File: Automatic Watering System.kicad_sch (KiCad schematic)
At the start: 6 parts, among them J1 691137710002, J2 691137710002, U1 DFR0654

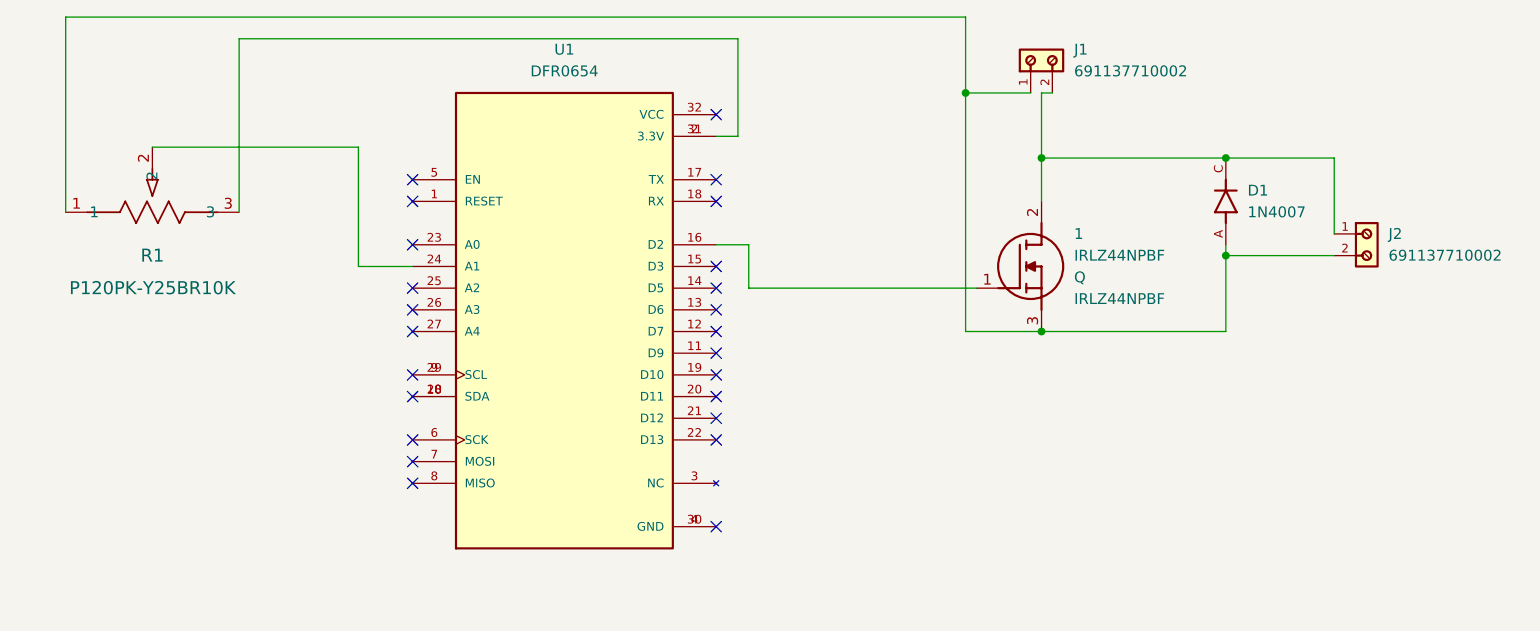
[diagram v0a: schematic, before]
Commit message: Fixing some issues with schematics and changing potentiometer
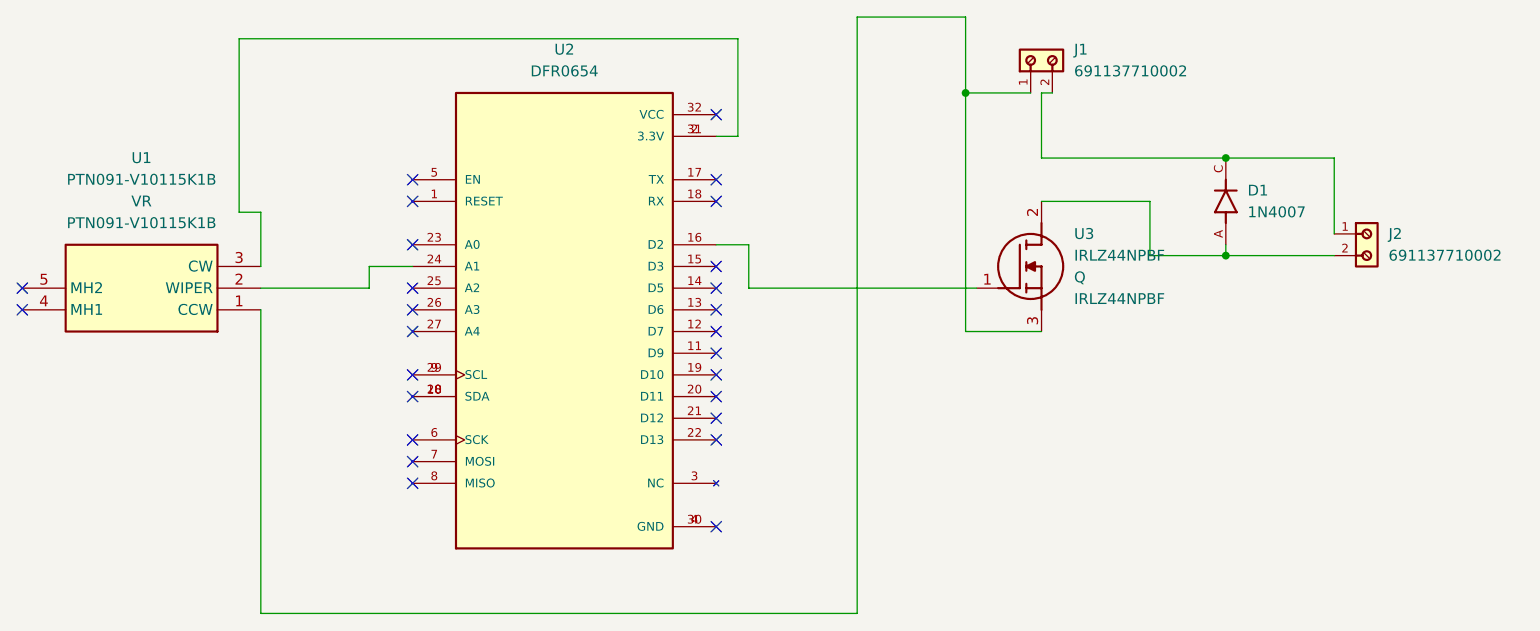
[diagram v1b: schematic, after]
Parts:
- removed R1: P120PK-Y25BR10K, Imported:POT_P120PK-x25_TTE, symbol Imported:P120PK-Y25BR10K
- added U1: PTN091-V10115K1B, Imported:PTN091V10115K1B, symbol Imported:PTN091-V10115K1B
- renumbered U1 to U2, 1 to U3
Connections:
- net at U2.2 (3.3V), U2.31 (3.3V): now also U1.3 (CW)
- net at U2.24 (A1): now also U1.2 (WIPER)
- net at D1.C, J1.2, J2.1: no longer U3.2 (D)
- net at J1.1, U3.3 (S): now also U1.1 (CCW); no longer D1.A, J2.2
- new net: D1.A, J2.2, U3.2 (D)
- no-connect marks 24 -> 26
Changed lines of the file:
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@@
 (kicad_sch (version 20211123) (generator eeschema)
   (paper "A4")
-  (junction (at 133.35 60.96) (diameter 0) (color 0 0 0 0)
-  )
-  (junction (at 133.35 40.64) (diameter 0) (color 0 0 0 0)
+  (junction (at 154.94 52.07) (diameter 0) (color 0 0 0 0)
   )
   (junction (at 154.94 40.64) (diameter 0) (color 0 0 0 0)
-  )
-  (junction (at 154.94 52.07) (diameter 0) (color 0 0 0 0)
   )
   (junction (at 124.46 33.02) (diameter 0) (color 0 0 0 0)
@@
   (no_connect (at 59.69 78.74))
   (no_connect (at 59.69 68.58))
+  (no_connect (at 13.97 55.88))
   (no_connect (at 95.25 45.72))
   (no_connect (at 59.69 66.04))
@@
   (no_connect (at 59.69 50.8))
   (no_connect (at 95.25 58.42))
+  (no_connect (at 13.97 58.42))
   (no_connect (at 95.25 68.58))
   (no_connect (at 95.25 55.88))
   (no_connect (at 59.69 45.72))
-  (wire (pts (xy 53.34 39.37) (xy 53.34 53.34))
-    (stroke (width 0) (type default) (color 0 0 0 0))
-  )
   (wire (pts (xy 39.37 46.99) (xy 39.37 26.67))
     (stroke (width 0) (type default) (color 0 0 0 0))
@@
     (stroke (width 0) (type default) (color 0 0 0 0))
   )
-  (wire (pts (xy 19.05 24.13) (xy 124.46 24.13))
+  (wire (pts (xy 39.37 46.99) (xy 41.91 46.99))
+    (stroke (width 0) (type default) (color 0 0 0 0))
+  )
+  (wire (pts (xy 54.61 55.88) (xy 54.61 53.34))
+    (stroke (width 0) (type default) (color 0 0 0 0))
+  )
+  (wire (pts (xy 41.91 55.88) (xy 54.61 55.88))
     (stroke (width 0) (type default) (color 0 0 0 0))
   )
@@
     (stroke (width 0) (type default) (color 0 0 0 0))
   )
+  (wire (pts (xy 111.76 24.13) (xy 124.46 24.13))
+    (stroke (width 0) (type default) (color 0 0 0 0))
+  )
   (wire (pts (xy 124.46 24.13) (xy 124.46 33.02))
     (stroke (width 0) (type default) (color 0 0 0 0))
@@
     (stroke (width 0) (type default) (color 0 0 0 0))
   )
+  (wire (pts (xy 146.05 45.72) (xy 133.35 45.72))
+    (stroke (width 0) (type default) (color 0 0 0 0))
+  )
   (wire (pts (xy 154.94 40.64) (xy 167.64 40.64))
     (stroke (width 0) (type default) (color 0 0 0 0))
@@
     (stroke (width 0) (type default) (color 0 0 0 0))
   )
+  (wire (pts (xy 41.91 46.99) (xy 41.91 53.34))
+    (stroke (width 0) (type default) (color 0 0 0 0))
+  )
   (wire (pts (xy 99.06 50.8) (xy 95.25 50.8))
     (stroke (width 0) (type default) (color 0 0 0 0))
   )
-  (wire (pts (xy 133.35 45.72) (xy 133.35 40.64))
-    (stroke (width 0) (type default) (color 0 0 0 0))
-  )
-  (wire (pts (xy 19.05 46.99) (xy 19.05 24.13))
-    (stroke (width 0) (type default) (color 0 0 0 0))
-  )
   (wire (pts (xy 133.35 33.02) (xy 134.62 33.02))
     (stroke (width 0) (type default) (color 0 0 0 0))
   )
-  (wire (pts (xy 29.21 39.37) (xy 53.34 39.37))
-    (stroke (width 0) (type default) (color 0 0 0 0))
-  )
-  (wire (pts (xy 154.94 60.96) (xy 133.35 60.96))
+  (wire (pts (xy 54.61 53.34) (xy 59.69 53.34))
+    (stroke (width 0) (type default) (color 0 0 0 0))
+  )
+  (wire (pts (xy 111.76 93.98) (xy 111.76 24.13))
     (stroke (width 0) (type default) (color 0 0 0 0))
   )
@@
     (stroke (width 0) (type default) (color 0 0 0 0))
   )
-  (wire (pts (xy 154.94 52.07) (xy 154.94 60.96))
+  (wire (pts (xy 146.05 52.07) (xy 146.05 45.72))
     (stroke (width 0) (type default) (color 0 0 0 0))
   )
@@
     (stroke (width 0) (type default) (color 0 0 0 0))
   )
+  (wire (pts (xy 41.91 93.98) (xy 111.76 93.98))
+    (stroke (width 0) (type default) (color 0 0 0 0))
+  )
   (wire (pts (xy 39.37 26.67) (xy 97.79 26.67))
     (stroke (width 0) (type default) (color 0 0 0 0))
@@
     (stroke (width 0) (type default) (color 0 0 0 0))
   )
-  (wire (pts (xy 53.34 53.34) (xy 59.69 53.34))
+  (wire (pts (xy 41.91 58.42) (xy 41.91 93.98))
     (stroke (width 0) (type default) (color 0 0 0 0))
   )
@@
     (stroke (width 0) (type default) (color 0 0 0 0))
   )
+  (wire (pts (xy 154.94 52.07) (xy 146.05 52.07))
+    (stroke (width 0) (type default) (color 0 0 0 0))
+  )
   (symbol (lib_id "Imported:DFR0654") (at 77.47 58.42 0) (unit 1)
     (in_bom yes) (on_board yes) (fields_autoplaced)
-    (property "Reference" "U1" (id 0) (at 77.47 27.94 0))
+    (property "Reference" "U2" (id 0) (at 77.47 27.94 0))
     (property "Value" "DFR0654" (id 1) (at 77.47 30.48 0))
     (property "Footprint" "Imported:MODULE_DFR0654" (id 2) (at 77.47 58.42 0)
@@
     (pin "9")
   )
+  (symbol (lib_id "Imported:PTN091-V10115K1B") (at 41.91 58.42 180) (unit 1)
+    (in_bom yes) (on_board yes) (fields_autoplaced)
+    (property "Reference" "U1" (id 0) (at 27.94 40.64 0))
+    (property "Value" "PTN091-V10115K1B" (id 1) (at 27.94 43.18 0))
+    (property "Footprint" "Imported:PTN091V10115K1B" (id 2) (at 41.91 58.42 0)
+      (effects (font (size 1.27 1.27)) hide)
+    )
+    (property "Datasheet" "" (id 3) (at 41.91 58.42 0)
+      (effects (font (size 1.27 1.27)) hide)
+    )
+    (property "Reference_1" "VR" (id 4) (at 27.94 45.72 0))
+    (property "Value_1" "PTN091-V10115K1B" (id 5) (at 27.94 48.26 0))
+    (property "Footprint_1" "PTN091V10115K1B" (id 6) (at 17.78 -36.5 0)
+      (effects (font (size 1.27 1.27)) (justify left top) hide)
+    )
+    (property "Datasheet_1" "https://www.sameskydevices.com/product/resource/supplyframepdf/ptn09x.pdf" (id 7) (at 17.78 -136.5 0)
+      (effects (font (size 1.27 1.27)) (justify left top) hide)
+    )
+    (property "Height" "24.7" (id 8) (at 17.78 -336.5 0)
+      (effects (font (size 1.27 1.27)) (justify left top) hide)
+    )
+    (property "Mouser Part Number" "179-PTN091V10115K1B" (id 9) (at 17.78 -436.5 0)
+      (effects (font (size 1.27 1.27)) (justify left top) hide)
+    )
+    (property "Mouser Price/Stock" "https://www.mouser.co.uk/ProductDetail/Same-Sky/PTN091-V10115K1B?qs=IKkN%2F947nfDKcGbyc2sMDg%3D%3D" (id 10) (at 17.78 -536.5 0)
+      (effects (font (size 1.27 1.27)) (justify left top) hide)
+    )
+    (property "Manufacturer_Name" "Same Sky" (id 11) (at 17.78 -636.5 0)
+      (effects (font (size 1.27 1.27)) (justify left top) hide)
+    )
+    (property "Manufacturer_Part_Number" "PTN091-V10115K1B" (id 12) (at 17.78 -736.5 0)
+      (effects (font (size 1.27 1.27)) (justify left top) hide)
+    )
+    (pin "1")
+    (pin "2")
+    (pin "3")
+    (pin "4")
+    (pin "5")
+  )
   (symbol (lib_id "Imported:691137710002") (at 172.72 52.07 270) (unit 1)
     (in_bom yes) (on_board yes) (fields_autoplaced)
@@
   (symbol (lib_id "Imported:IRLZ44NPBF") (at 125.73 55.88 0) (unit 1)
     (in_bom yes) (on_board yes) (fields_autoplaced)
-    (property "Reference" "1" (id 0) (at 137.16 49.5299 0)
+    (property "Reference" "U3" (id 0) (at 137.16 49.5299 0)
       (effects (font (size 1.27 1.27)) (justify left))
     )
@@
     (pin "C")
   )
-  (symbol (lib_id "Imported:P120PK-Y25BR10K") (at 19.05 46.99 0) (unit 1)
-    (in_bom yes) (on_board yes) (fields_autoplaced)
-    (property "Reference" "R1" (id 0) (at 29.21 52.07 0)
-      (effects (font (size 1.524 1.524)))
-    )
-    (property "Value" "P120PK-Y25BR10K" (id 1) (at 29.21 55.88 0)
-      (effects (font (size 1.524 1.524)))
-    )
-    (property "Footprint" "Imported:POT_P120PK-x25_TTE" (id 2) (at 19.05 46.99 0)
-      (effects (font (size 1.27 1.27) italic) hide)
-    )
-    (property "Datasheet" "P120PK-Y25BR10K" (id 3) (at 19.05 46.99 0)
-      (effects (font (size 1.27 1.27) italic) hide)
-    )
-    (pin "1")
-    (pin "2")
-    (pin "3")
-  )
   (symbol (lib_id "Imported:691137710002") (at 134.62 27.94 0) (unit 1)
     (in_bom yes) (on_board yes) (fields_autoplaced)
@@
   )
   (symbol_instances
-    (path "/ba70a276-afbb-439b-9f33-0dd4e2613e4b"
-      (reference "1") (unit 1) (value "IRLZ44NPBF") (footprint "Imported:TO254P469X1042X1967-3P")
-    )
     (path "/e58e873f-b633-4e2e-9ff7-a71404a8971e"
       (reference "D1") (unit 1) (value "1N4007") (footprint "Imported:DIOAD1060W80L520D270")
@@
       (reference "J2") (unit 1) (value "691137710002") (footprint "Imported:691137710002")
     )
-    (path "/e83c7425-e1d2-47ea-91f0-522ac990ae42"
-      (reference "R1") (unit 1) (value "P120PK-Y25BR10K") (footprint "Imported:POT_P120PK-x25_TTE")
+    (path "/4e00a6b8-30b0-4f4f-a94c-57583c41a87d"
+      (reference "U1") (unit 1) (value "PTN091-V10115K1B") (footprint "Imported:PTN091V10115K1B")
     )
     (path "/3a37f798-dd51-4b0d-a169-8740e743fd1c"
-      (reference "U1") (unit 1) (value "DFR0654") (footprint "Imported:MODULE_DFR0654")
-    )
-  )
+      (reference "U2") (unit 1) (value "DFR0654") (footprint "Imported:MODULE_DFR0654")
+    )
+    (path "/ba70a276-afbb-439b-9f33-0dd4e2613e4b"
+      (reference "U3") (unit 1) (value "IRLZ44NPBF") (footprint "Imported:TO254P469X1042X1967-3P")
+    )
+  )
